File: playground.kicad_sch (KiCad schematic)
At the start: 21 parts, among them IC1 TXU0101DBVR, IC2 TXU0101DBVR, IC3 TXU0101DBVR, IC4 TXU0101DBVR, IC5 TXU0101DBVR, IC6 TXU0101DBVR, IC7 TXU0101DBVR, IC8 TXU0101DBVR, J1 USB_A, SW1 SW_DIP_x01, U2 ATSAMD21G18A-A

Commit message: updates
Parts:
- removed IC1, IC2, IC3, IC4, IC5, IC6, IC7, IC8: TXU0101DBVR, custom_footprints:TXU0101DBVR, symbol custom_symbols:TXU0101DBVR
- removed J1: USB_A, Connector_USB:USB3_A_Receptacle_Wuerth_692122030100, symbol Connector:USB_A
- added IC9: L293DD, custom_footprints:SOIC127P1032X265-20N, symbol custom_symbols:L293DD
- added J2: Pump, custom_footprints:470531000, symbol custom_symbols:47053-1000
- added J3: Fan, custom_footprints:470531000, symbol custom_symbols:47053-1000
- added J4: Valve, custom_footprints:470531000, symbol custom_symbols:47053-1000
- added J6: MOLEX POWER CONNECTOR, custom_footprints:455580003, symbol custom_symbols:45558-0003
- added J7: USB_A, Connector_USB:USB_A_Molex_67643_Horizontal, symbol Connector:USB_A
- C1, C2: footprint Capacitor_SMD:CP_Elec_8x10 -> Capacitor_SMD:C_0805_2012Metric
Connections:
- net +5V: now also IC9.1 (ENABLE_1), IC9.11 (ENABLE_2), IC9.20 (VSS), J7.1 (VBUS)
- net FanSense_5v: now also J3.3
- net GND: now also IC9.14 (GND_5), IC9.15 (GND_6), IC9.16 (GND_7), IC9.17 (GND_8), IC9.4 (GND_1), IC9.5 (GND_2), IC9.6 (GND_3), IC9.7 (GND_4), J6.4, J6.5, J6.6, J7.4 (GND)
- net PumpCtrl_5v: now also J2.4
- net PumpSense_5v: now also J2.3
- net USB_D+: now also J7.3 (D+)
- net USB_D-: now also J7.2 (D-)
- net ValveCtrl1_5v: now also IC9.2 (INPUT_1)
- net ValveCtrl2_5v: now also IC9.9 (INPUT_2)
- net usb_shield_gnd: now also J7.5 (Shield)
- new net +12V: IC9.10 (VS), J6.1, J6.2, J6.3
- new net FanCtrl_5v: J3.4
- new net ValveOutput1_5v: IC9.3 (OUTPUT_1)
- new net ValveOutput2_5v: IC9.8 (OUTPUT_2)
- no-connect marks 29 -> 37
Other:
- added sheet Power Regulation (power_regulation.kicad_sch)
- added sheet level_shifters (level_shifters.kicad_sch)
- note added: "Level Shifter"
- note added: "MOLEX POWER"
- note added: "Peripheral Ports"
- note added: "Valve Controller"
- note removed: "FanCtrlShifter"
- note removed: "PumpCtrlShifter"
- note removed: "PumpSeneShifter"
- note removed: "ValveCtrl1Shifter"
- note removed: "ValveCtrl2Shifter"
- moved on the sheet: C1, R1, R2, SW1, U2

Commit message: did basic routing. Still missing some parts.
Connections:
- net ValveOutput1_5v is gone; now on net ValveOutput1_12v: IC9.3 (OUTPUT_1)
- net ValveOutput2_5v is gone; now on net ValveOutput2_12v: IC9.8 (OUTPUT_2)
- net +5V: no longer D1.1 (K), D2.1 (K), D5.1 (K), J7.1 (VBUS)
- net ValveSense1_5v: now also J4.2
- net ValveSense2_5v: now also J4.1
- net ValveOutput1_12v: now reaches J4.3
- net ValveOutput2_12v: now reaches J4.4
- new net USB_VBUS: D1.1 (K), D2.1 (K), D5.1 (K), J7.1 (VBUS)
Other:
- note added: "NOTE: Not using USB Power."
- moved on the sheet: J2, J3, J4

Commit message: saving progress
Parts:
- added C10, C11: 10u, Capacitor_SMD:C_0805_2012Metric, symbol Device:C
- added C12, C13: 20p, Capacitor_SMD:C_0805_2012Metric, symbol Device:C
- added C3: 4.7n, Capacitor_SMD:C_0805_2012Metric, symbol Device:C
- added C4, C6, C7: 100n, Capacitor_SMD:C_0805_2012Metric, symbol Device:C
- added C5: 47u, Capacitor_SMD:C_0805_2012Metric, symbol Device:C
- added C8, C9: 1u, Capacitor_SMD:C_0805_2012Metric, symbol Device:C
- added D10: FAN_PWM_IND, LED_SMD:LED_0603_1608Metric, symbol Device:LED
- added D11: VALVE_OPEN_IND, LED_SMD:LED_0603_1608Metric, symbol Device:LED
- added D12: VALVE_CLOSED_IND, LED_SMD:LED_0603_1608Metric, symbol Device:LED
- added D13, D14: GENERAL_BOARD_1_IND, LED_SMD:LED_0603_1608Metric, symbol Device:LED
- added D6: 5V_USB_PWR_IND, LED_SMD:LED_0603_1608Metric, symbol Device:LED
- added D7: 3v3_PWR_IND, LED_SMD:LED_0603_1608Metric, symbol Device:LED
- added D8: 12v_PWR_IND, LED_SMD:LED_0603_1608Metric, symbol Device:LED
- added D9: PUMP_PWM_IND, LED_SMD:LED_0603_1608Metric, symbol Device:LED
- added IC11: LM3940IMP-3.3_NOPB, custom_footprints:SOT230P700X180-4N, symbol custom_symbols:LM3940IMP-3.3_NOPB
- added J5: Conn_02x05_Counter_Clockwise, Connector_PinHeader_2.54mm:PinHeader_2x05_P2.54mm_Vertical_SMD, symbol Connector_Generic:Conn_02x05_Counter_Clockwise
- added JP1, JP2: SolderJumper_2_Open, Jumper:SolderJumper-2_P1.3mm_Open_Pad1.0x1.5mm, symbol Jumper:SolderJumper_2_Open
- added R4: 1k, Resistor_SMD:R_0805_2012Metric, symbol Device:R
- added R5: 51R, Resistor_SMD:R_0805_2012Metric, symbol Device:R
- added R6, R7: 470R, Resistor_SMD:R_0805_2012Metric, symbol Device:R
- added R8: 300R, Resistor_SMD:R_1206_3216Metric, symbol Device:R
- added Y1: 32.768kHz, custom_footprints:FC135327680KAA5, symbol custom_symbols:FC-135_32.7680KA-A5
- C1: value C -> 100n
- J7: footprint Connector_USB:USB_A_Molex_67643_Horizontal -> custom_footprints:676432910
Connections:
- net USB_VBUS is gone; now on net +5V: D1.1 (K), D2.1 (K), D5.1 (K), J7.1 (VBUS)
- net +12V: now also D8.2 (A), R6.2
- net +3V3: now also C10.1, C11.1, C4.1, C6.1, C7.1, C8.1, C9.1, D7.2 (A), J5.1 (Pin_1), JP2.2 (B), R4.2, R5.2
- net +5V: now also JP1.1 (A)
- net GND: now also C10.2, C11.2, C12.1, C13.1, C3.2, C4.2, C5.2, C6.2, C7.2, C8.2, C9.2, D10.1 (K), D11.1 (K), D12.1 (K), D13.1 (K), D14.1 (K), D6.1 (K), D7.1 (K), D8.1 (K), D9.1 (K), IC11.2 (GND_1), IC11.4 (GND_2), J5.2 (Pin_2), J5.3 (Pin_3), R5.1, R7.2
- net RESET: now also J5.6 (Pin_6)
- net XIN32: now reaches U2.1 (PA00)
- net XIN32: now also C13.2, Y1.2
- net XOUT32: now reaches U2.2 (PA01)
- net XOUT32: now also C12.2, Y1.1
- net SWCLK: now reaches U2.45 (PA30)
- net SWCLK: now also J5.9 (Pin_9), R4.1
- net SWDIO: now reaches U2.46 (PA31)
- net SWDIO: now also J5.10 (Pin_10)
- new net: R6.1, R7.1, R8.1
- new net 5v_USB_PWR_IND_LED: D6.2 (A)
- new net FAN_PWM_IND_LED: D10.2 (A)
- new net GENERAL_BOARD_1_IND_LED: D13.2 (A), D14.2 (A)
- new net LDO_POWER_IN: C3.1, IC11.1 (IN), JP1.2 (B)
- new net LDO_POWER_OUT: C5.1, IC11.3 (OUT), JP2.1 (A)
- new net PUMP_PWM_IND_LED: D9.2 (A)
- new net VALVE_CLOSED_IND_LED: D12.2 (A)
- new net VALVE_OPEN_IND_LED: D11.2 (A)
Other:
- removed sheet Power Regulation
- note added: "(NOTE: might modify this)"
- note added: "5V to 3v3 regulator"
- note added: "Close Decoupling Caps"
- note added: "Debug / Indicator LEDs"
- note added: "Further Decoupling Caps"
- note added: "LED Connections"
- note added: "MCU Crystal"
- note added: "MCU Decoupling Caps"
- note added: "MCU SWD"

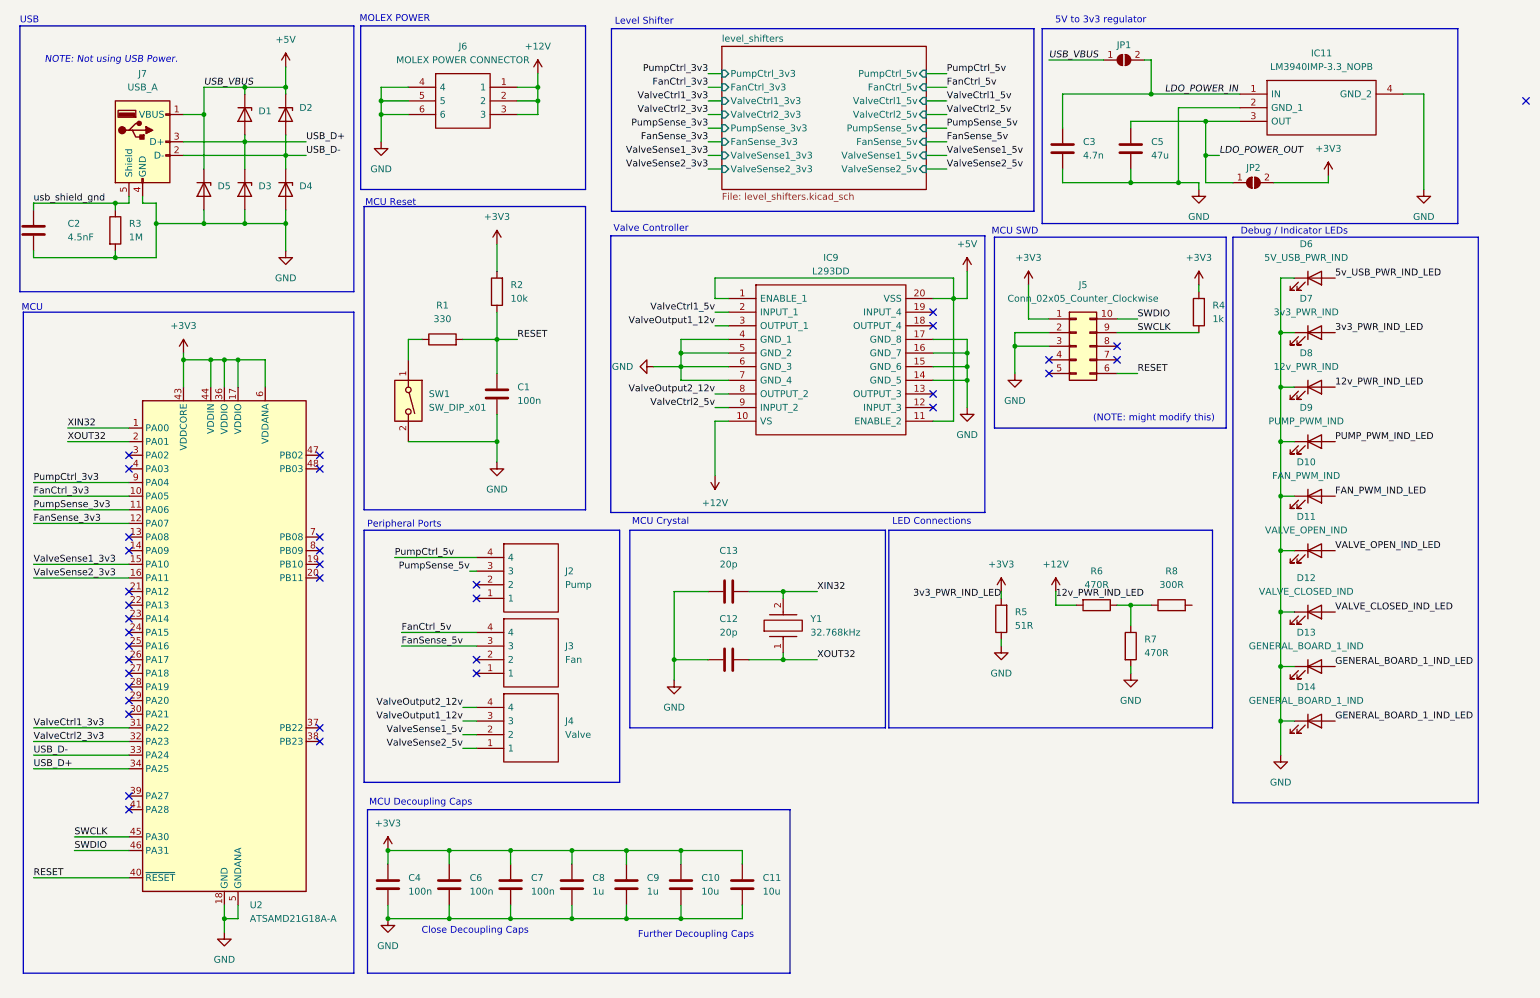
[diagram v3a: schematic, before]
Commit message: Added LEDs and testpoints
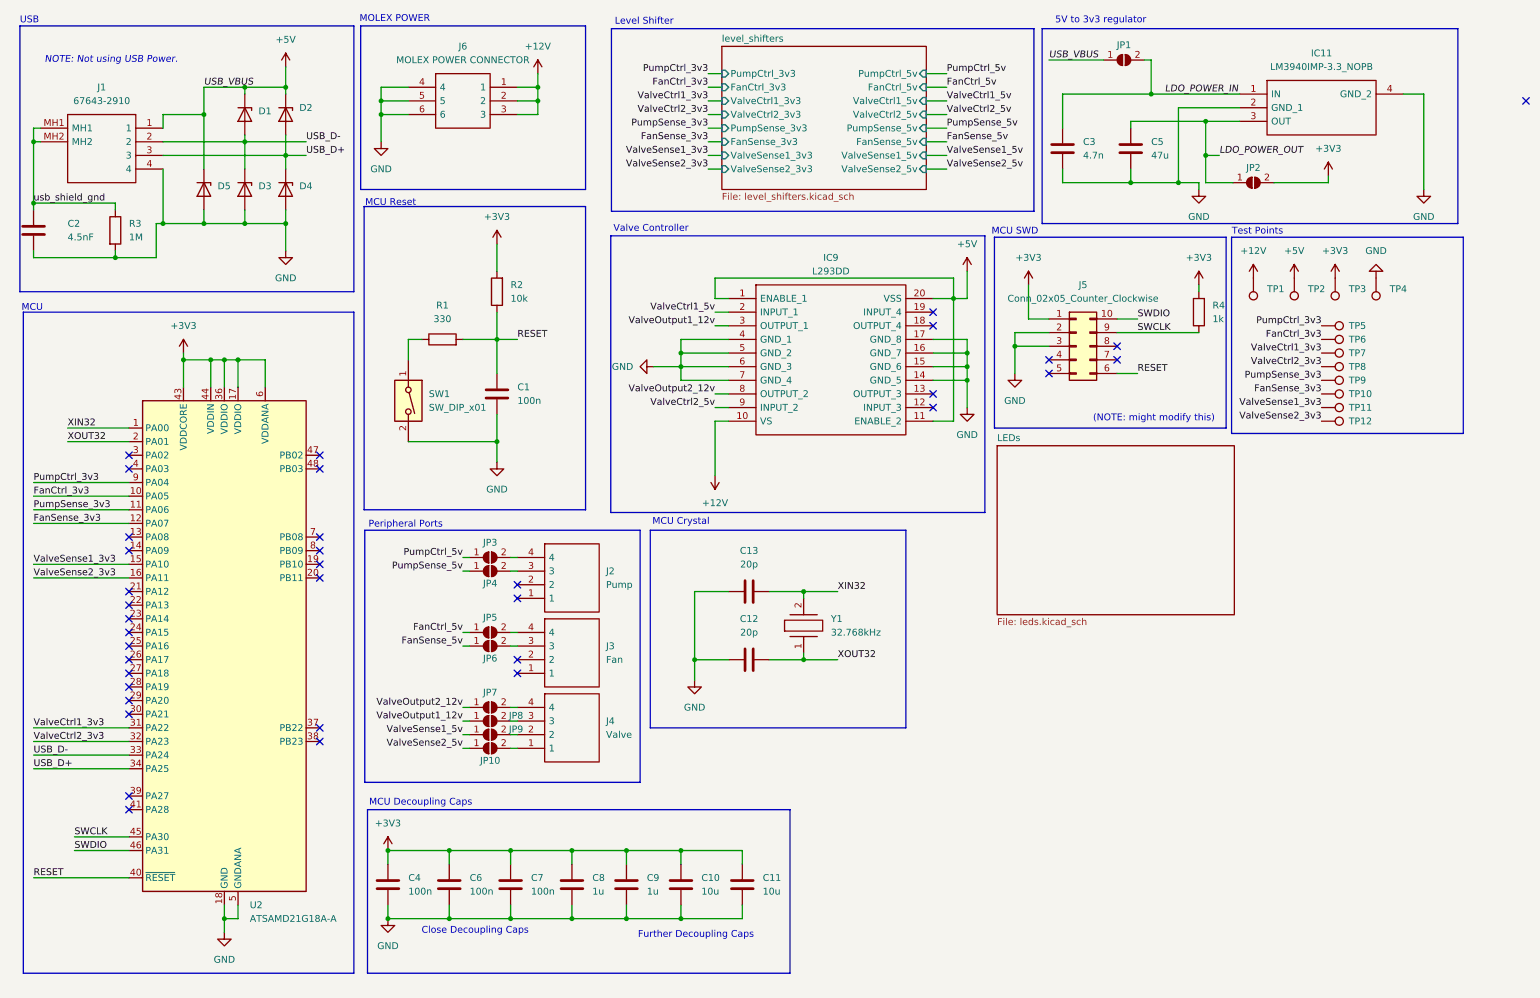
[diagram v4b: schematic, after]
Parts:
- removed D10: FAN_PWM_IND, LED_SMD:LED_0603_1608Metric, symbol Device:LED
- removed D11: VALVE_OPEN_IND, LED_SMD:LED_0603_1608Metric, symbol Device:LED
- removed D12: VALVE_CLOSED_IND, LED_SMD:LED_0603_1608Metric, symbol Device:LED
- removed D13, D14: GENERAL_BOARD_1_IND, LED_SMD:LED_0603_1608Metric, symbol Device:LED
- removed D6: 5V_USB_PWR_IND, LED_SMD:LED_0603_1608Metric, symbol Device:LED
- removed D7: 3v3_PWR_IND, LED_SMD:LED_0603_1608Metric, symbol Device:LED
- removed D8: 12v_PWR_IND, LED_SMD:LED_0603_1608Metric, symbol Device:LED
- removed D9: PUMP_PWM_IND, LED_SMD:LED_0603_1608Metric, symbol Device:LED
- removed J7: USB_A, custom_footprints:676432910, symbol Connector:USB_A
- removed R5: 51R, Resistor_SMD:R_0805_2012Metric, symbol Device:R
- removed R6, R7: 470R, Resistor_SMD:R_0805_2012Metric, symbol Device:R
- removed R8: 300R, Resistor_SMD:R_1206_3216Metric, symbol Device:R
- added J1: 67643-2910, custom_footprints:676432910, symbol custom_symbols:67643-2910
- added JP10, JP3, JP4, JP5, JP6, JP7, JP8, JP9: SolderJumper_2_Open, Jumper:SolderJumper-2_P1.3mm_Open_Pad1.0x1.5mm, symbol Jumper:SolderJumper_2_Open
- added TP1, TP10, TP11, TP12, TP2, TP3, TP4, TP5, TP6, TP7, TP8, TP9: TestPoint, TestPoint:TestPoint_Pad_D2.0mm, symbol Connector:TestPoint
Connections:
- net +12V: now also TP1.1
- net +3V3: now also TP3.1
- net +5V: now also J1.1, TP2.1
- net FanCtrl_3v3: now also TP6.1
- net FanCtrl_5v: now also JP5.1 (A); no longer J3.4
- net FanSense_3v3: now also TP10.1
- net FanSense_5v: now also JP6.1 (A); no longer J3.3
- net GND: now also J1.4, TP4.1
- net PumpCtrl_3v3: now also TP5.1
- net PumpCtrl_5v: now also JP3.1 (A); no longer J2.4
- net PumpSense_3v3: now also TP9.1
- net PumpSense_5v: now also JP4.1 (A); no longer J2.3
- net USB_D+: now also D2.2 (A), D4.1 (K), J1.3; no longer D1.2 (A), D3.1 (K)
- net USB_D-: now also D1.2 (A), D3.1 (K), J1.2; no longer D2.2 (A), D4.1 (K)
- net ValveCtrl1_3v3: now also TP7.1
- net ValveCtrl2_3v3: now also TP8.1
- net ValveOutput1_12v: now also JP8.1 (A); no longer J4.3
- net ValveOutput2_12v: now also JP7.1 (A); no longer J4.4
- net ValveSense1_3v3: now also TP11.1
- net ValveSense1_5v: now also JP9.1 (A); no longer J4.2
- net ValveSense2_3v3: now also TP12.1
- net ValveSense2_5v: now also JP10.1 (A); no longer J4.1
- net usb_shield_gnd: now also J1.MH1, J1.MH2
- new net: J4.2, JP9.2 (B)
- new net: J2.3, JP4.2 (B)
- new net: J2.4, JP3.2 (B)
- new net: J4.3, JP8.2 (B)
- new net: J4.4, JP7.2 (B)
- new net: J4.1, JP10.2 (B)
- new net: J3.4, JP5.2 (B)
- new net: J3.3, JP6.2 (B)
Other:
- added sheet LEDs (leds.kicad_sch)
- note added: "Test Points"
- note removed: "Debug / Indicator LEDs"
- note removed: "LED Connections"
- moved on the sheet: C12, C13, J2, J3, J4, Y1

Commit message: removed jumpers
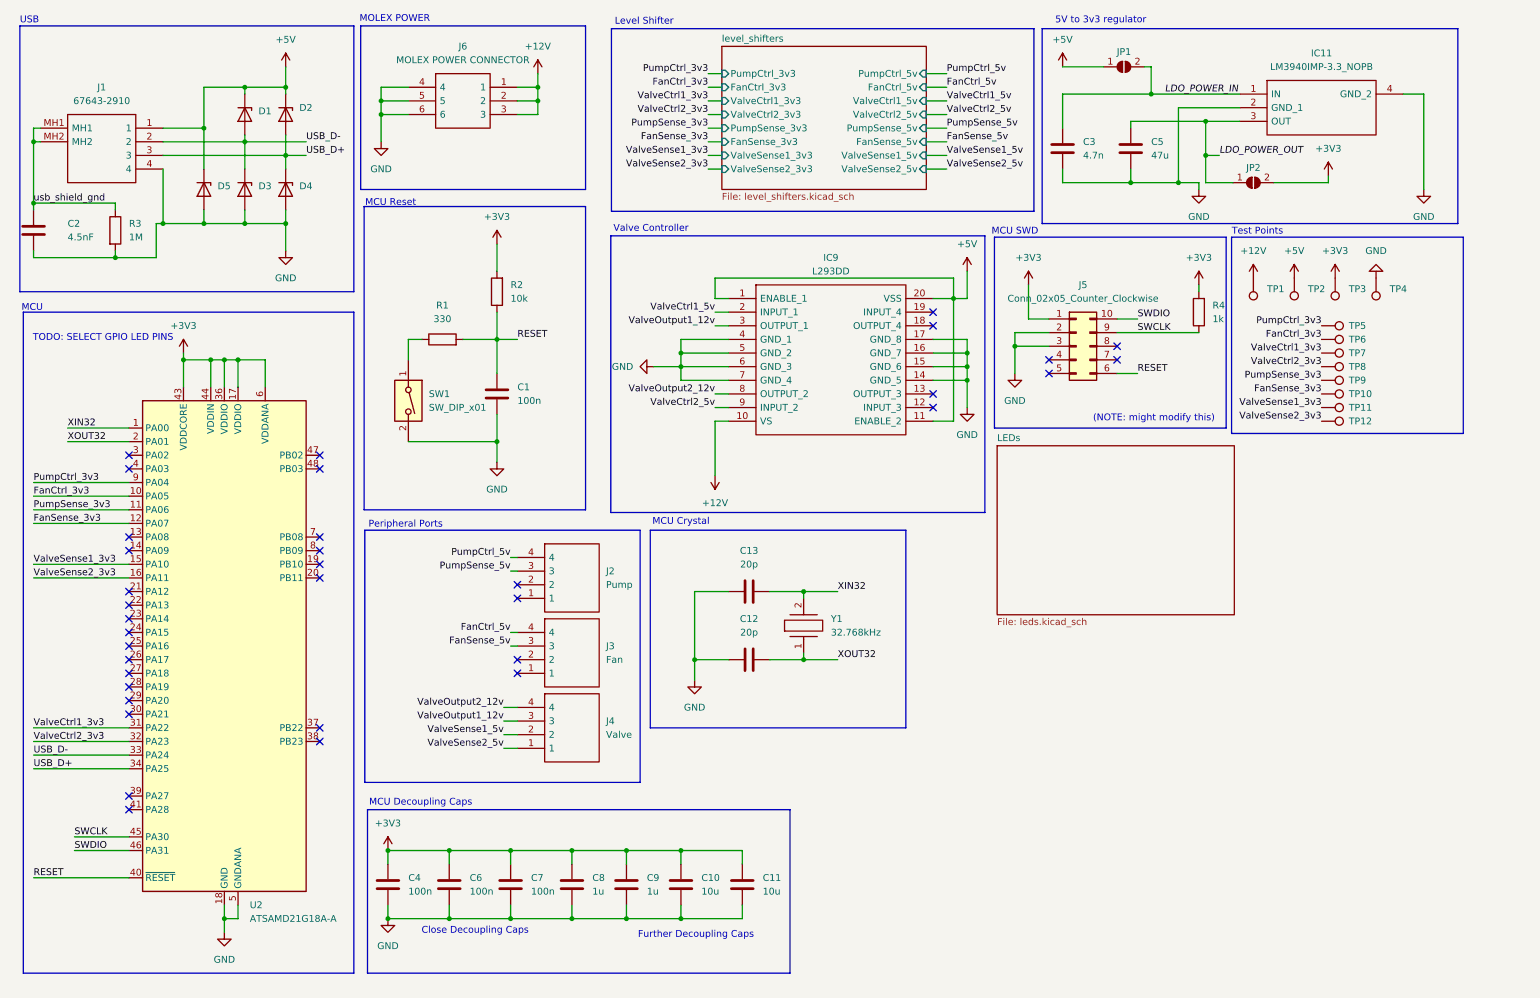
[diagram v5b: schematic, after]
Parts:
- removed JP10, JP3, JP4, JP5, JP6, JP7, JP8, JP9: SolderJumper_2_Open, Jumper:SolderJumper-2_P1.3mm_Open_Pad1.0x1.5mm, symbol Jumper:SolderJumper_2_Open
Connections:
- net FanCtrl_5v: now also J3.4
- net FanSense_5v: now also J3.3
- net PumpCtrl_5v: now also J2.4
- net PumpSense_5v: now also J2.3
- net ValveOutput1_12v: now also J4.3
- net ValveOutput2_12v: now also J4.4
- net ValveSense1_5v: now also J4.2
- net ValveSense2_5v: now also J4.1
- no-connect marks 37 -> 36
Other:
- note added: "TODO: SELECT GPIO LED PINS"
- note removed: "NOTE: Not using USB Power."
- moved on the sheet: JP1
